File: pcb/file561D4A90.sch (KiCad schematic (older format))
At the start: 50 parts, among them P10 CONN_01X02, P11 CONN_01X02, Q10 BC849, Q11 IRF9530, Q12 BC849, Q13 CSD18536KCS, Q14 BC849, Q15 IRF9530, Q16 BC849, Q17 CSD18536KCS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

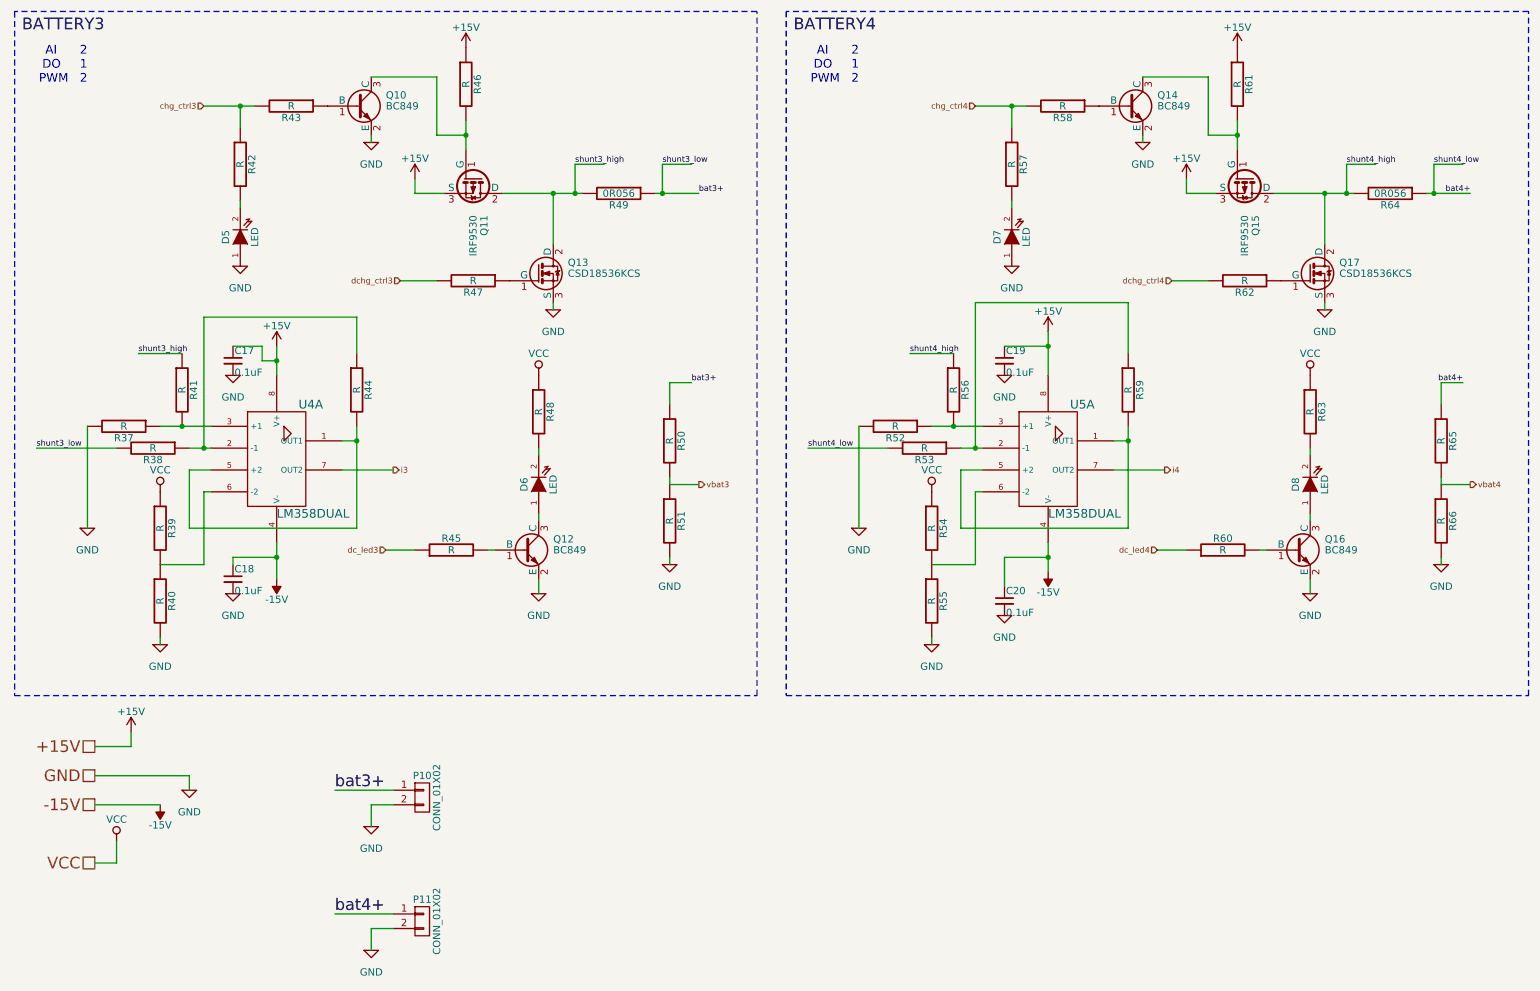
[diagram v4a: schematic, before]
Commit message: Changed fan FET (Q22). Many other minor layout changes. Production candidate.
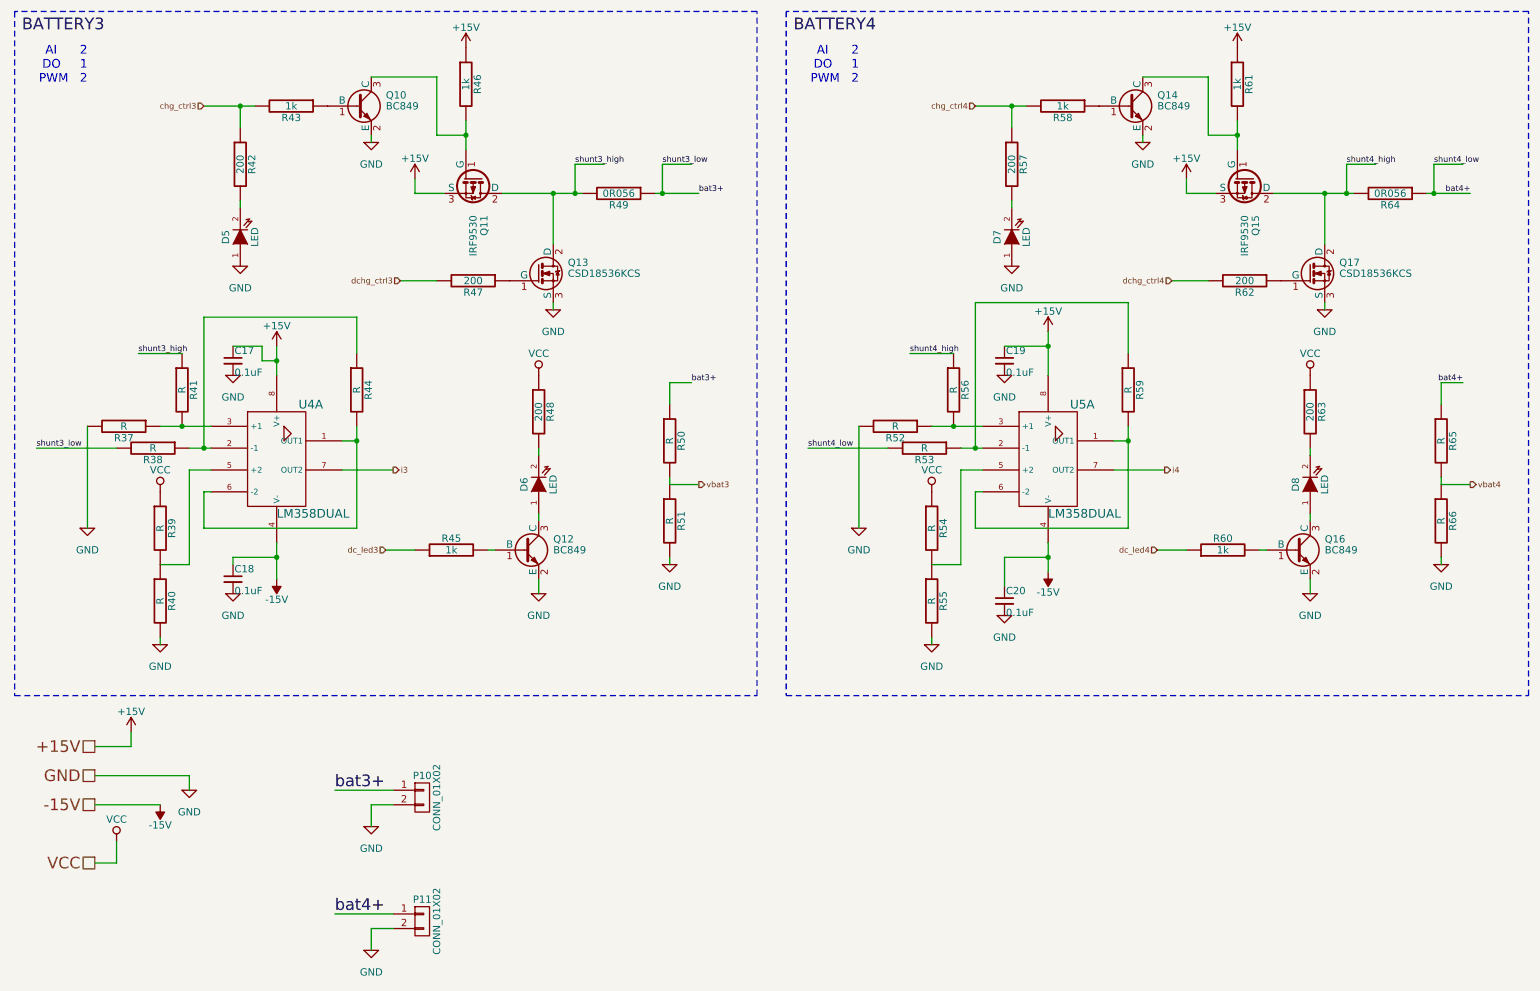
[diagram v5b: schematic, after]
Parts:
- Q11, Q13, Q15, Q17: footprint Power_Integrations:TO-220 -> Custom Footprints:TO-220
- R42, R47, R48, R57, R62, R63: value R -> 200
- R43, R45, R46, R58, R60, R61: value R -> 1k
- R44: footprint Resistors_ThroughHole:Resistor_Horizontal_RM10mm -> Custom Footprints:Resistor_Horizontal_RM10mm
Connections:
- net at R44.2, U4.1 (OUT1): now also U4.6 (-2); no longer U4.5 (+2)
- net at R39.2, R40.1: now also U4.5 (+2); no longer U4.6 (-2)
- net at R59.2, U5.1 (OUT1): now also U5.6 (-2); no longer U5.5 (+2)
- net at R54.2, R55.1: now also U5.5 (+2); no longer U5.6 (-2)
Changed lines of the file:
@@
 F 0 "Q13" H 4400 2425 50  0000 L CNN
 F 1 "CSD18536KCS" H 4400 2350 50  0000 L CNN
-F 2 "Power_Integrations:TO-220" H 4400 2275 50  0001 L CIN
+F 2 "Custom Footprints:TO-220" H 4400 2275 50  0001 L CIN
 F 3 "" H 4200 2350 50  0000 L CNN
 	1    4200 2350
@@
 F 0 "Q11" H 4000 1775 50  0000 L CNN
 F 1 "IRF9530" H 4000 1700 50  0000 L CNN
-F 2 "Power_Integrations:TO-220" H 4000 1625 50  0001 L CIN
+F 2 "Custom Footprints:TO-220" H 4000 1625 50  0001 L CIN
 F 3 "" H 3750 1700 50  0000 L CNN
 	1    3750 1700
@@
 P 4200 3300
 F 0 "R48" V 4280 3300 50  0000 C CNN
-F 1 "R" V 4200 3300 50  0000 C CNN
+F 1 "200" V 4200 3300 50  0000 C CNN
 F 2 "Resistors_SMD:R_0805_HandSoldering" V 4130 3300 30  0001 C CNN
 F 3 "" H 4200 3300 30  0000 C CNN
@@
 P 2150 1600
 F 0 "R42" V 2230 1600 50  0000 C CNN
-F 1 "R" V 2150 1600 50  0000 C CNN
+F 1 "200" V 2150 1600 50  0000 C CNN
 F 2 "Resistors_SMD:R_0805_HandSoldering" V 2080 1600 30  0001 C CNN
 F 3 "" H 2150 1600 30  0000 C CNN
@@
 P 3700 1050
 F 0 "R46" V 3780 1050 50  0000 C CNN
-F 1 "R" V 3700 1050 50  0000 C CNN
+F 1 "1k" V 3700 1050 50  0000 C CNN
 F 2 "Resistors_SMD:R_0805_HandSoldering" V 3630 1050 30  0001 C CNN
 F 3 "" H 3700 1050 30  0000 C CNN
@@
 P 2500 1200
 F 0 "R43" V 2580 1200 50  0000 C CNN
-F 1 "R" V 2500 1200 50  0000 C CNN
+F 1 "1k" V 2500 1200 50  0000 C CNN
 F 2 "Resistors_SMD:R_0805_HandSoldering" V 2430 1200 30  0001 C CNN
 F 3 "" H 2500 1200 30  0000 C CNN
@@
 P 3750 2400
 F 0 "R47" V 3830 2400 50  0000 C CNN
-F 1 "R" V 3750 2400 50  0000 C CNN
+F 1 "200" V 3750 2400 50  0000 C CNN
 F 2 "Resistors_SMD:R_0805_HandSoldering" V 3680 2400 30  0001 C CNN
 F 3 "" H 3750 2400 30  0000 C CNN
@@
 P 3600 4250
 F 0 "R45" V 3680 4250 50  0000 C CNN
-F 1 "R" V 3600 4250 50  0000 C CNN
+F 1 "1k" V 3600 4250 50  0000 C CNN
 F 2 "Resistors_SMD:R_0805_HandSoldering" V 3530 4250 30  0001 C CNN
 F 3 "" H 3600 4250 30  0000 C CNN
@@
 F 0 "R44" V 3030 3150 50  0000 C CNN
 F 1 "R" V 2950 3150 50  0000 C CNN
-F 2 "Resistors_ThroughHole:Resistor_Horizontal_RM10mm" V 2880 3150 30  0001 C CNN
+F 2 "Custom Footprints:Resistor_Horizontal_RM10mm" V 2880 3150 30  0001 C CNN
 F 3 "" H 2950 3150 30  0000 C CNN
 	1    2950 3150
@@
 	1300 3550 750  3550
 Wire Wire Line
-	2950 4100 1800 4100
-Wire Wire Line
-	1800 4100 1800 3700
+	1800 3700 1800 4350
 Wire Wire Line
 	1800 3700 1950 3700
@@
 Wire Wire Line
 	1950 3850 1900 3850
-Wire Wire Line
-	1900 3850 1900 4350
-Wire Wire Line
-	1900 4350 1600 4350
 Wire Wire Line
 	1600 4900 1600 4850
@@
 F 0 "Q17" H 9700 2425 50  0000 L CNN
 F 1 "CSD18536KCS" H 9700 2350 50  0000 L CNN
-F 2 "Power_Integrations:TO-220" H 9700 2275 50  0001 L CIN
+F 2 "Custom Footprints:TO-220" H 9700 2275 50  0001 L CIN
 F 3 "" H 9500 2350 50  0000 L CNN
 	1    9500 2350
@@
 F 0 "Q15" H 9300 1775 50  0000 L CNN
 F 1 "IRF9530" H 9300 1700 50  0000 L CNN
-F 2 "Power_Integrations:TO-220" H 9300 1625 50  0001 L CIN
+F 2 "Custom Footprints:TO-220" H 9300 1625 50  0001 L CIN
 F 3 "" H 9050 1700 50  0000 L CNN
 	1    9050 1700
@@
 P 9500 3300
 F 0 "R63" V 9580 3300 50  0000 C CNN
-F 1 "R" V 9500 3300 50  0000 C CNN
+F 1 "200" V 9500 3300 50  0000 C CNN
 F 2 "Resistors_SMD:R_0805_HandSoldering" V 9430 3300 30  0001 C CNN
 F 3 "" H 9500 3300 30  0000 C CNN
@@
 P 7450 1600
 F 0 "R57" V 7530 1600 50  0000 C CNN
-F 1 "R" V 7450 1600 50  0000 C CNN
+F 1 "200" V 7450 1600 50  0000 C CNN
 F 2 "Resistors_SMD:R_0805_HandSoldering" V 7380 1600 30  0001 C CNN
 F 3 "" H 7450 1600 30  0000 C CNN
@@
 P 9000 1050
 F 0 "R61" V 9080 1050 50  0000 C CNN
-F 1 "R" V 9000 1050 50  0000 C CNN
+F 1 "1k" V 9000 1050 50  0000 C CNN
 F 2 "Resistors_SMD:R_0805_HandSoldering" V 8930 1050 30  0001 C CNN
 F 3 "" H 9000 1050 30  0000 C CNN
@@
 P 7800 1200
 F 0 "R58" V 7880 1200 50  0000 C CNN
-F 1 "R" V 7800 1200 50  0000 C CNN
+F 1 "1k" V 7800 1200 50  0000 C CNN
 F 2 "Resistors_SMD:R_0805_HandSoldering" V 7730 1200 30  0001 C CNN
 F 3 "" H 7800 1200 30  0000 C CNN
@@
 P 9050 2400
 F 0 "R62" V 9130 2400 50  0000 C CNN
-F 1 "R" V 9050 2400 50  0000 C CNN
+F 1 "200" V 9050 2400 50  0000 C CNN
 F 2 "Resistors_SMD:R_0805_HandSoldering" V 8980 2400 30  0001 C CNN
 F 3 "" H 9050 2400 30  0000 C CNN
@@
 P 8900 4250
 F 0 "R60" V 8980 4250 50  0000 C CNN
-F 1 "R" V 8900 4250 50  0000 C CNN
+F 1 "1k" V 8900 4250 50  0000 C CNN
 F 2 "Resistors_SMD:R_0805_HandSoldering" V 8830 4250 30  0001 C CNN
 F 3 "" H 8900 4250 30  0000 C CNN
@@
 	6600 3550 6050 3550
 Wire Wire Line
-	8250 4100 7100 4100
-Wire Wire Line
-	7100 4100 7100 3700
-Wire Wire Line
 	7100 3700 7250 3700
 Connection ~ 8250 3500
 Wire Wire Line
 	7250 3850 7200 3850
-Wire Wire Line
-	7200 3850 7200 4350
-Wire Wire Line
-	7200 4350 6900 4350
 Wire Wire Line
 	6900 4900 6900 4850
@@
 Text Label 10550 3100 2    40   ~ 0
 bat4+
+Wire Wire Line
+	1800 4350 1600 4350
+Wire Wire Line
+	2950 4100 1900 4100
+Wire Wire Line
+	1900 4100 1900 3850
+Wire Wire Line
+	7100 3700 7100 4350
+Wire Wire Line
+	7100 4350 6900 4350
+Wire Wire Line
+	8250 4100 7200 4100
+Wire Wire Line
+	7200 4100 7200 3850
 $EndSCHEMATC

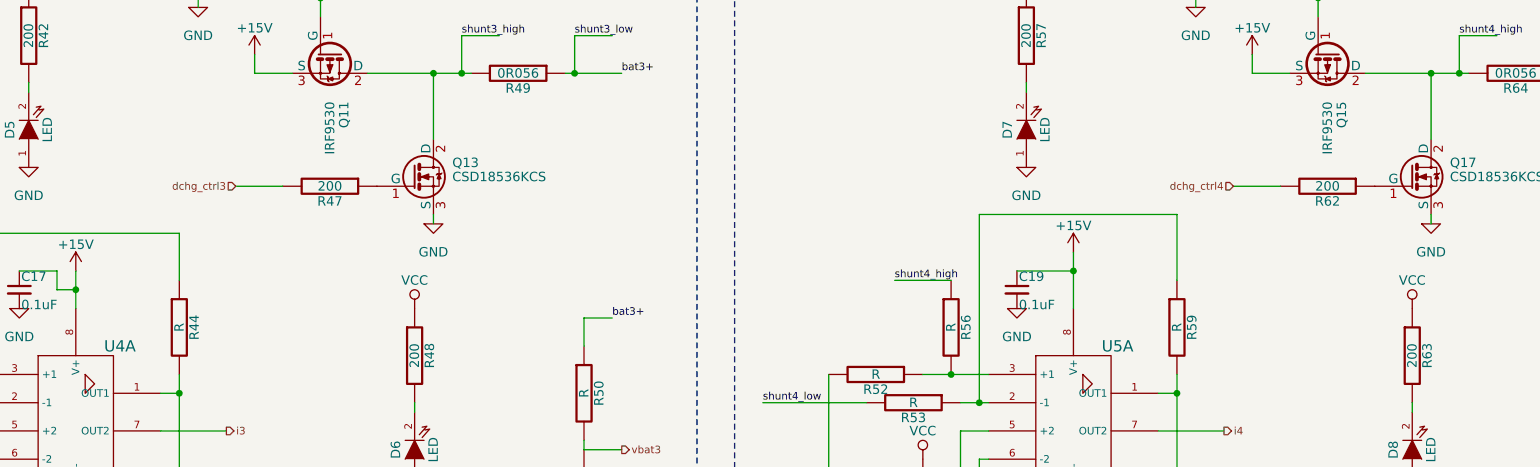
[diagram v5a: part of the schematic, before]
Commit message: Added caps on discharge fet gates
Need to filter the digital signal from the MCU to create an analog
voltage at the gate because the fet should operate in between on and
off states (which generates heat due to high Rds).
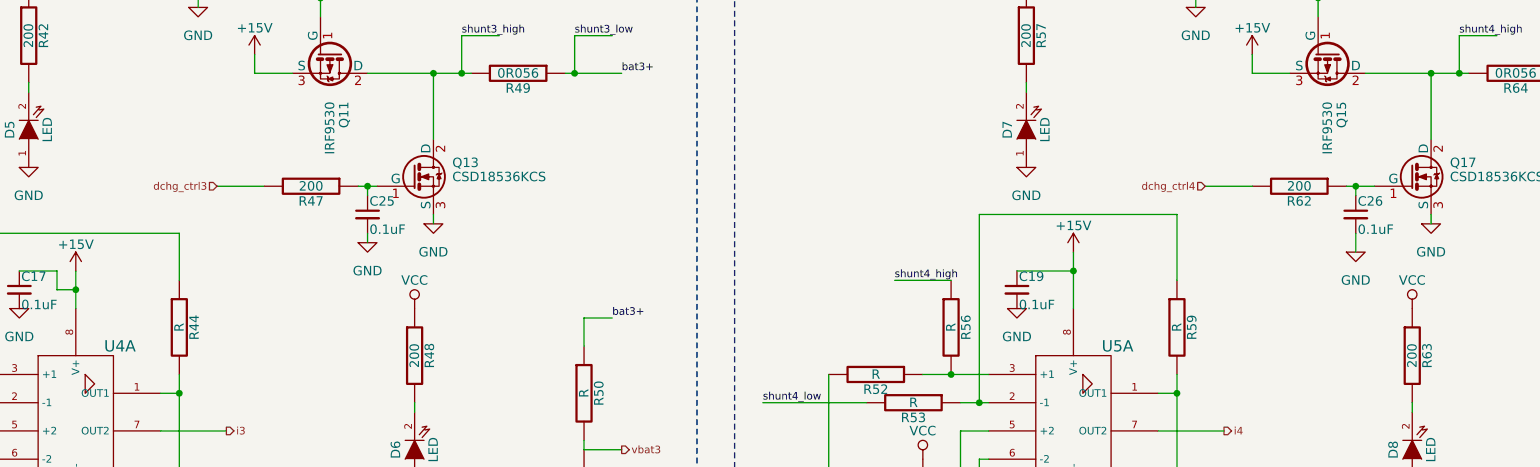
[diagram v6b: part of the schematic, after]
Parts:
- added C25, C26: 0.1uF, Capacitors_SMD:C_0805_HandSoldering, symbol C_Small
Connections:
- net GND: now also C25.2, C26.2
- net at Q13.1 (G), R47.1: now also C25.1
- net at Q17.1 (G), R62.1: now also C26.1
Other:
- moved on the sheet: R47, R62
